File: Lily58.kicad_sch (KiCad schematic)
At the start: 14 parts, among them J1 USB_C_Receptacle, U1 ESP32-S3-WROOM-2, U3 BQ24090DGQ, U4 AP63203WU, Y1 Crystal_GND24

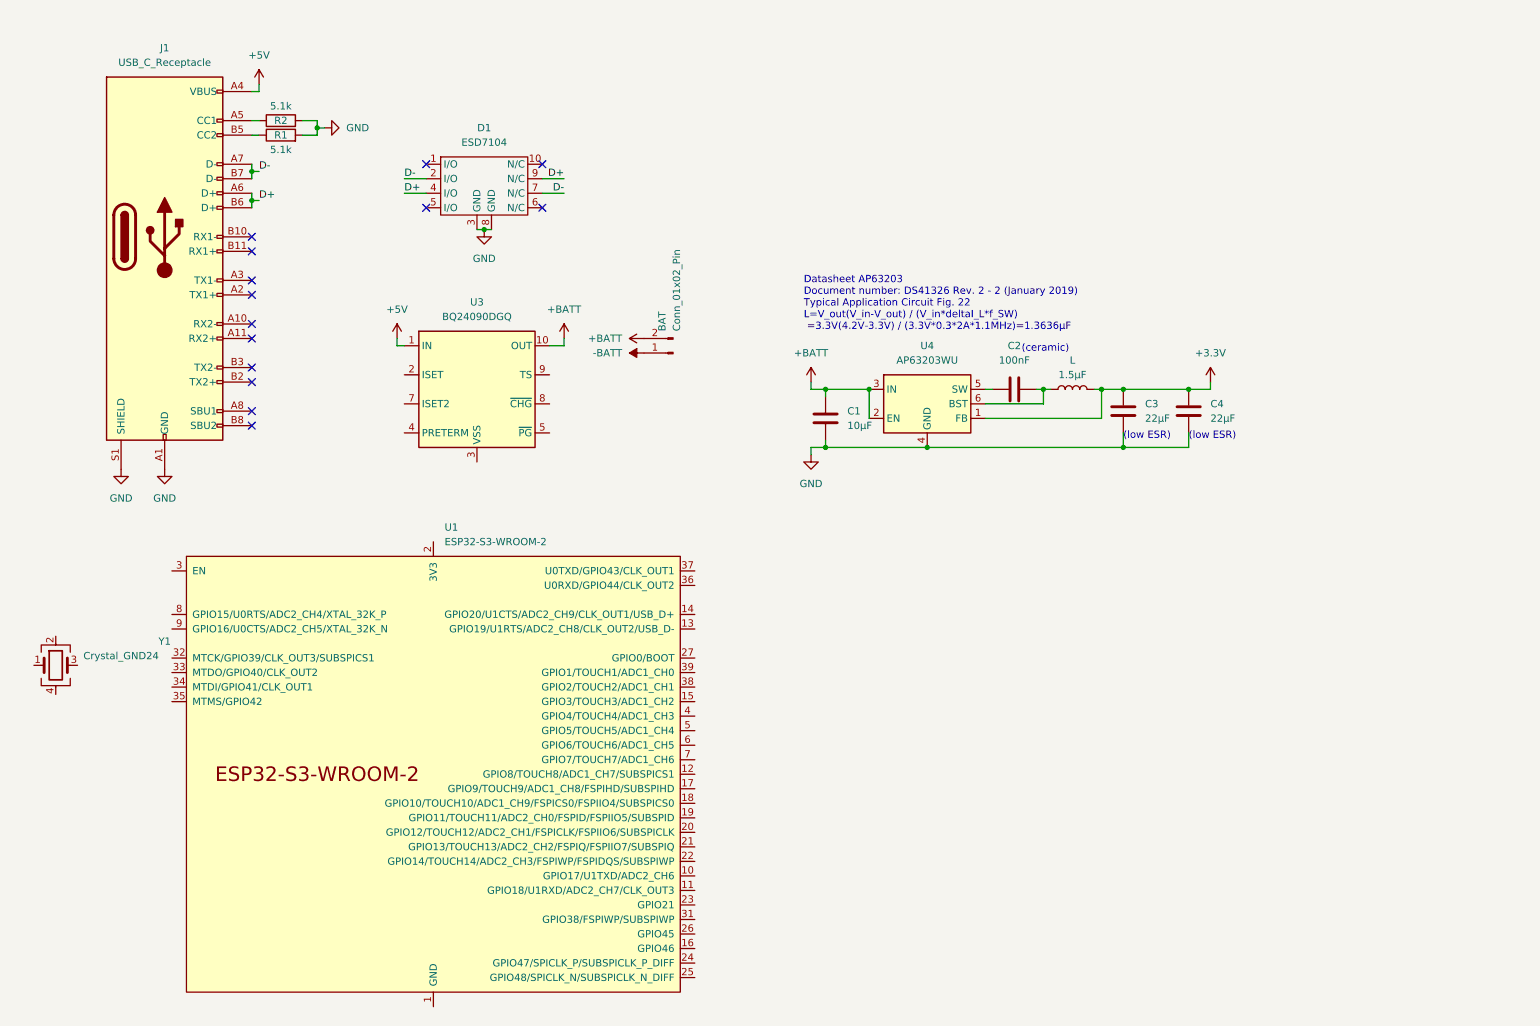
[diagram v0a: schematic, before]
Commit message: connected second USB-C receptacle; reorganized schematic
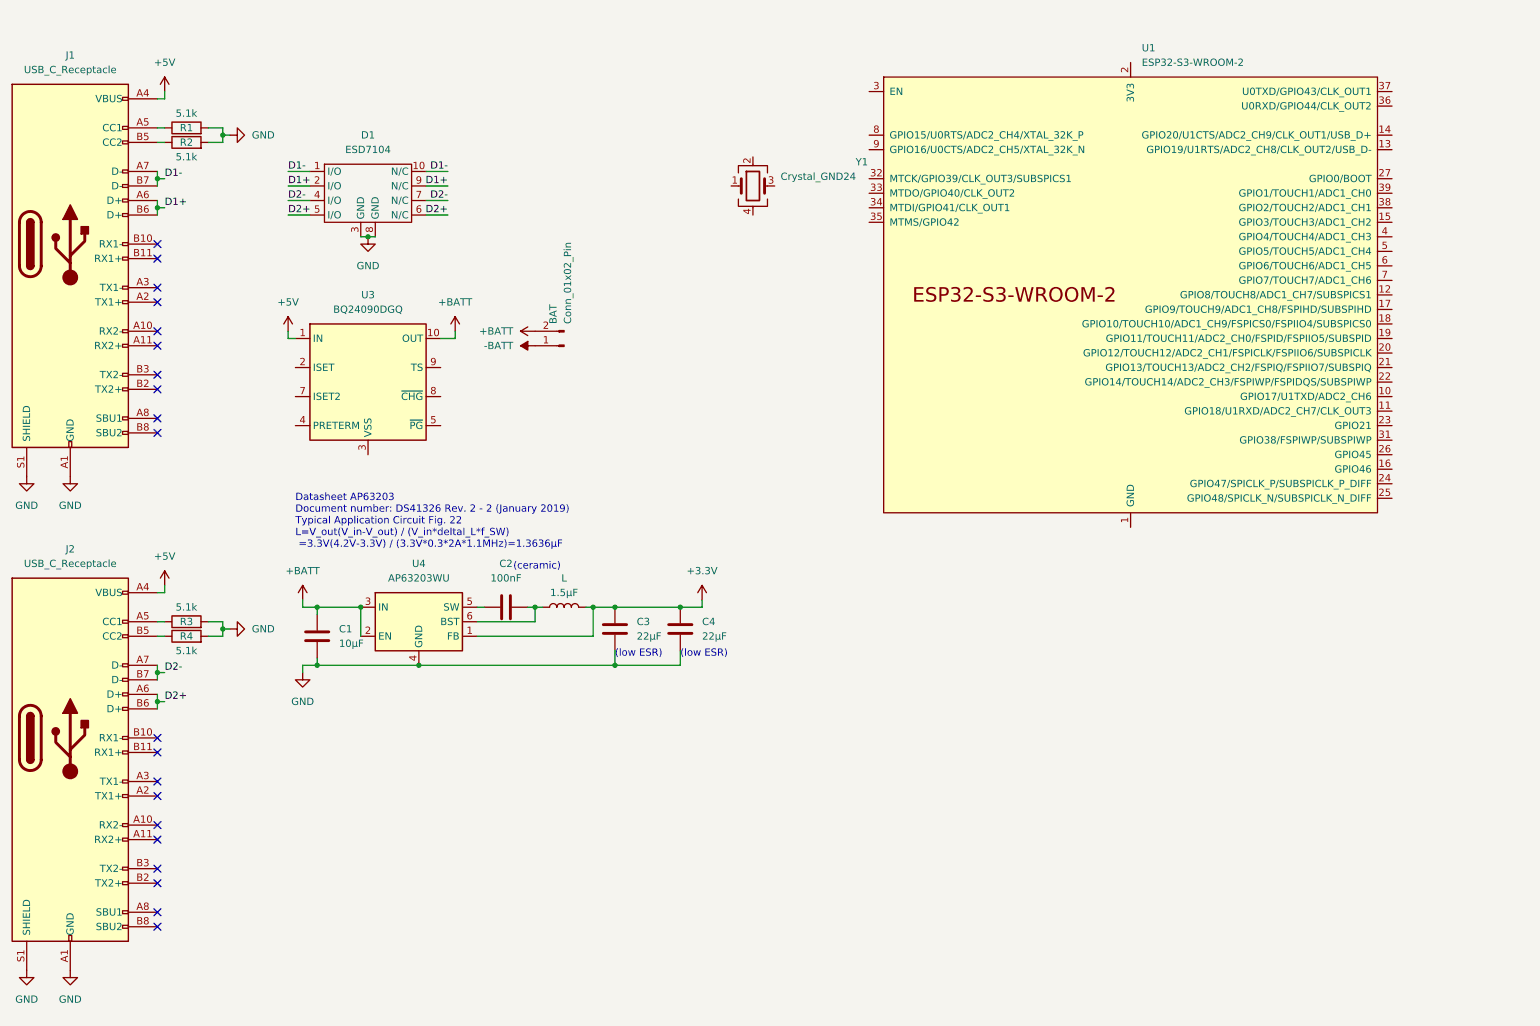
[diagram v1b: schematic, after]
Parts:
- added J2: USB_C_Receptacle, Connector_USB:USB_C_Receptacle_Amphenol_12401548E4-2A_CircularHoles, symbol Connector:USB_C_Receptacle
- added R3, R4: 5.1k, Resistor_SMD:R_0805_2012Metric_Pad1.20x1.40mm_HandSolder, symbol Device:R
- renumbered R2 to R1, R1 to R2
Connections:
- net +5V: now also J2.A4 (VBUS), J2.A9 (VBUS), J2.B4 (VBUS), J2.B9 (VBUS)
- net GND: now also J2.A1 (GND), J2.A12 (GND), J2.B1 (GND), J2.B12 (GND), J2.S1 (SHIELD), R3.2, R4.2
- net D1-: now reaches D1.1 (I/O)
- net D1-: now also D1.10 (N/C), J1.A7 (D-), J1.B7 (D-)
- net D2+: now reaches D1.5 (I/O)
- net D2+: now also D1.6 (N/C), J2.A6 (D+), J2.B6 (D+)
- net D+ renamed D1+
- net D1+: now also D1.2 (I/O); no longer D1.4 (I/O)
- removed net D-: D1.2 (I/O), D1.7 (N/C), J1.A7 (D-), J1.B7 (D-)
- new net: J2.A5 (CC1), R3.1
- new net: J2.B5 (CC2), R4.1
- new net D2-: D1.4 (I/O), D1.7 (N/C), J2.A7 (D-), J2.B7 (D-)
- no-connect marks 14 -> 20
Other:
- moved on the sheet: BAT, C1, C2, C3, C4, D1, J1, L, R1, R2, U1, U3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

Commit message: added level shifter and connected D+/D- with USB and I2C
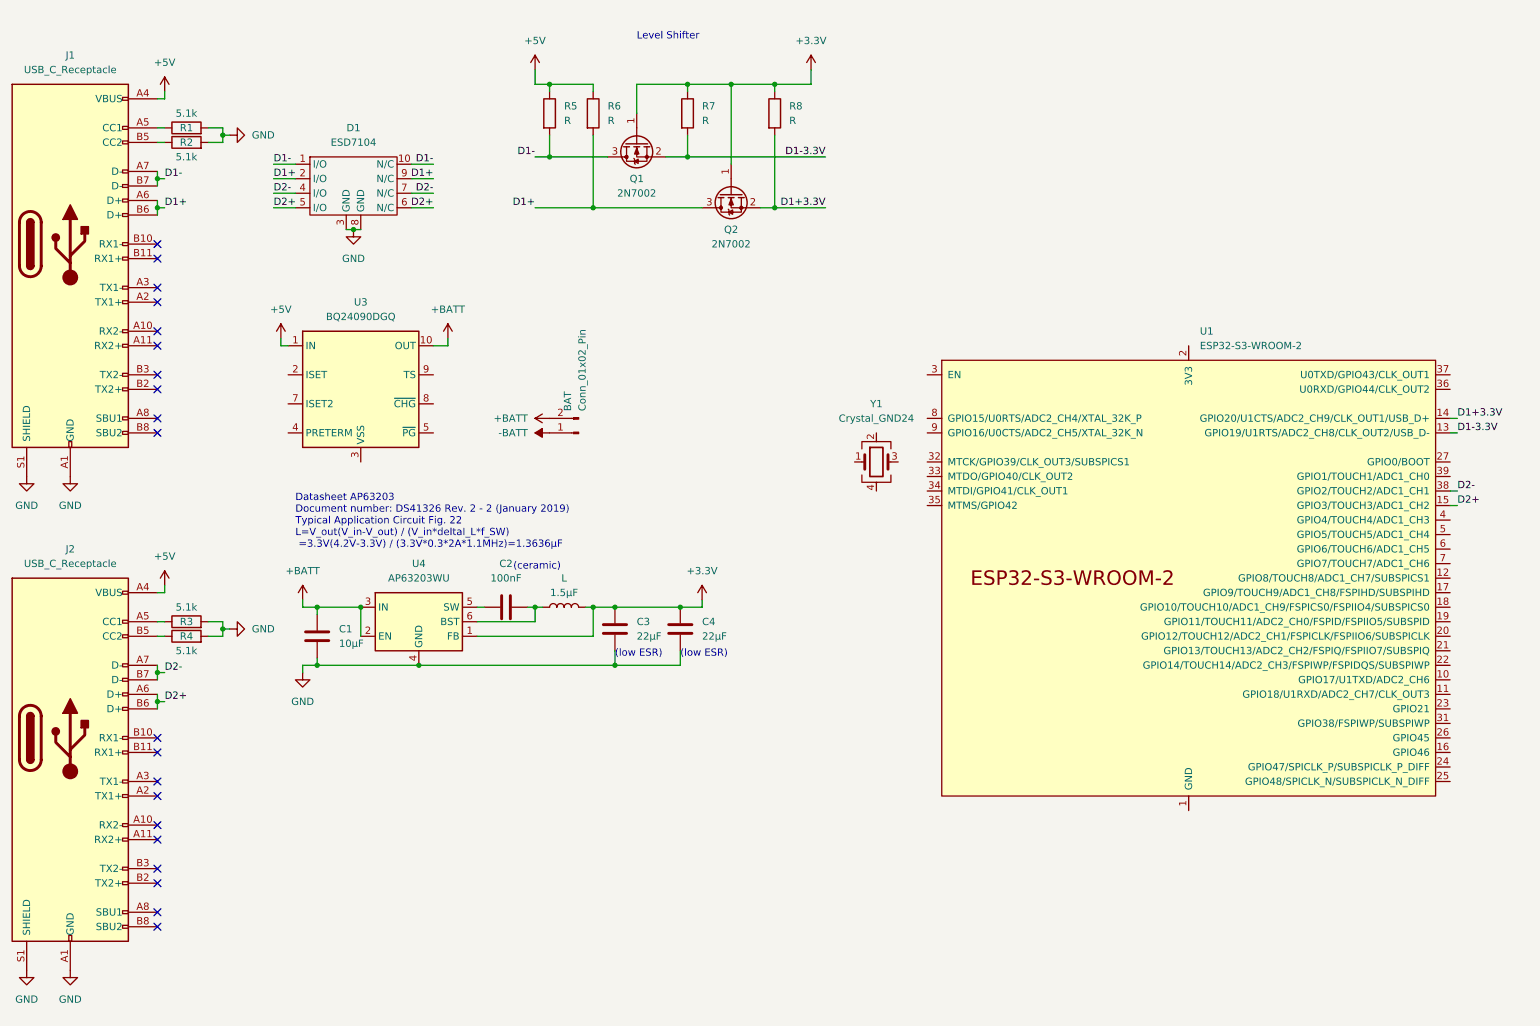
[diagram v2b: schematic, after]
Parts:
- added Q1, Q2: 2N7002, Package_TO_SOT_SMD:SOT-23, symbol Transistor_FET:2N7002
- added R5, R6, R7, R8: R, symbol Device:R
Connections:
- net +3.3V: now also Q1.1 (G), Q2.1 (G), R7.1, R8.1
- net +5V: now also R5.1, R6.1
- net D1+: now also Q2.3 (D), R6.2
- net D1-: now also Q1.3 (D), R5.2
- net D2+: now also U1.15 (GPIO3/TOUCH3/ADC1_CH2)
- net D2-: now also U1.38 (GPIO2/TOUCH2/ADC1_CH1)
- net D1-3.3V: now reaches U1.13 (GPIO19/U1RTS/ADC2_CH8/CLK_OUT2/USB_D-)
- net D1-3.3V: now also Q1.2 (S), R7.2
- net D1+3.3V: now reaches U1.14 (GPIO20/U1CTS/ADC2_CH9/CLK_OUT1/USB_D+)
- net D1+3.3V: now also Q2.2 (S), R8.2
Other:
- note added: "Level Shifter"
- moved on the sheet: BAT, D1, U1, U3, Y1

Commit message: added level shifters to second USB recaptacle for input protection
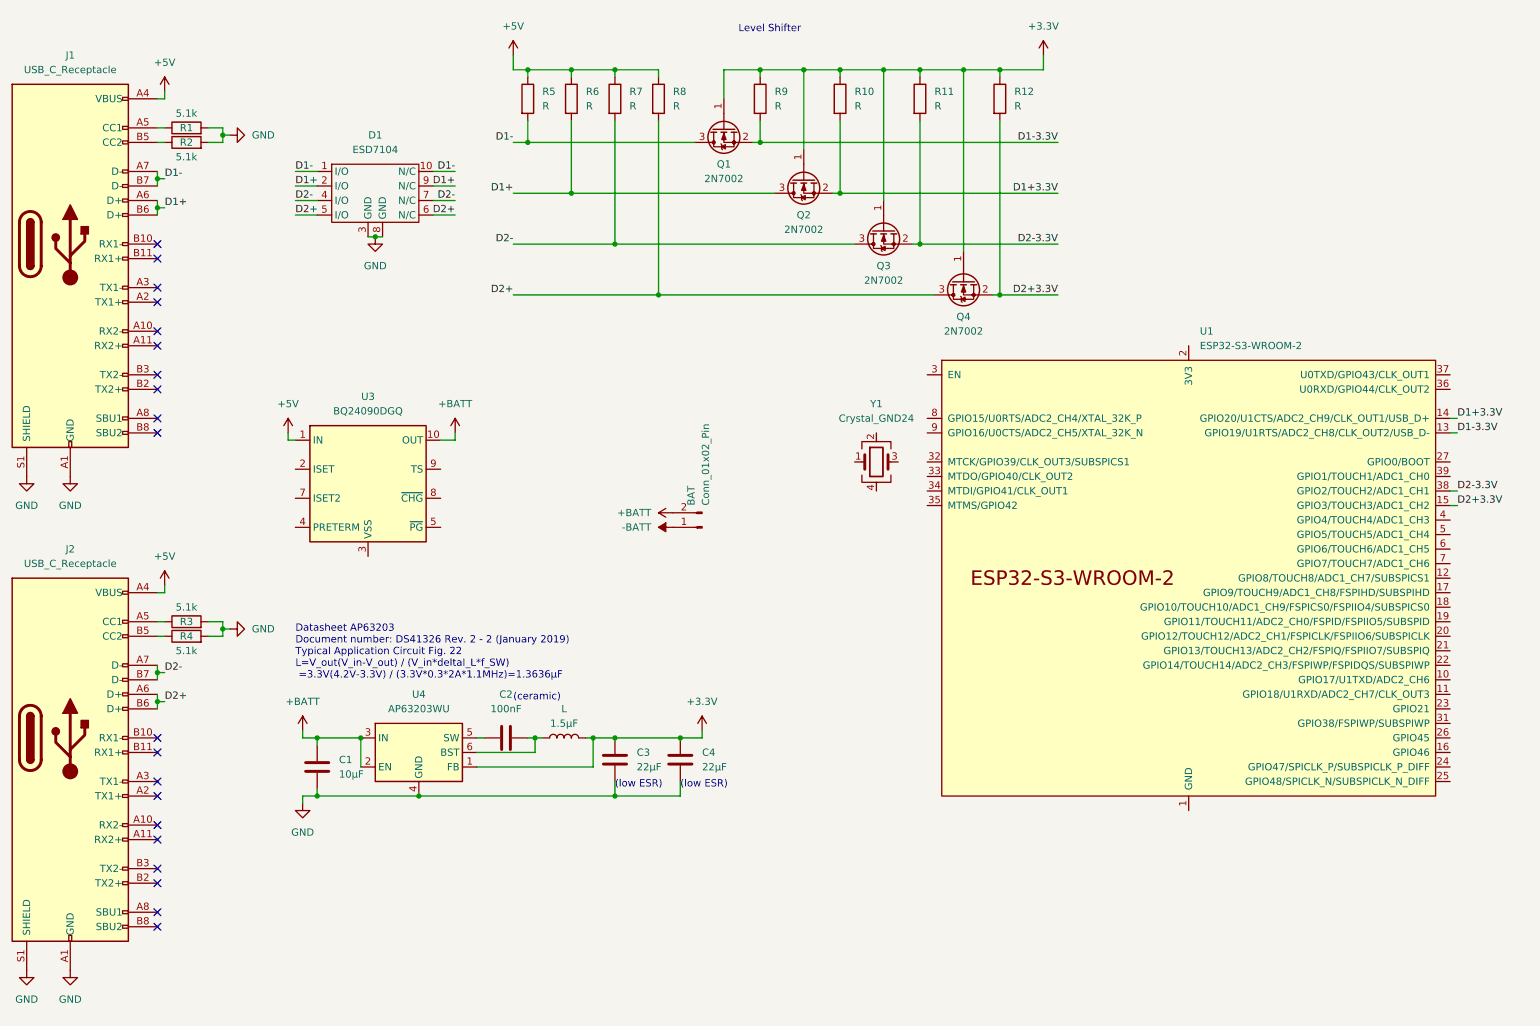
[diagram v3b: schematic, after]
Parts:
- added Q3, Q4: 2N7002, Package_TO_SOT_SMD:SOT-23, symbol Transistor_FET:2N7002
- added R11, R12, R7, R8: R, symbol Device:R
- renumbered R8 to R10, R7 to R9
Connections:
- net +3.3V: now also Q3.1 (G), Q4.1 (G), R11.1, R12.1
- net +5V: now also R7.1, R8.1
- net D2+: now also Q4.3 (D), R8.2; no longer U1.15 (GPIO3/TOUCH3/ADC1_CH2)
- net D2-: now also Q3.3 (D), R7.2; no longer U1.38 (GPIO2/TOUCH2/ADC1_CH1)
- new net D2+3.3V: Q4.2 (S), R12.2, U1.15 (GPIO3/TOUCH3/ADC1_CH2)
- new net D2-3.3V: Q3.2 (S), R11.2, U1.38 (GPIO2/TOUCH2/ADC1_CH1)
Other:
- moved on the sheet: BAT, C1, C2, C3, C4, D1, L, Q1, Q2, R10, R5, R6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

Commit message: changed AP63201 to TPS63001; added TPS63001 datasheet
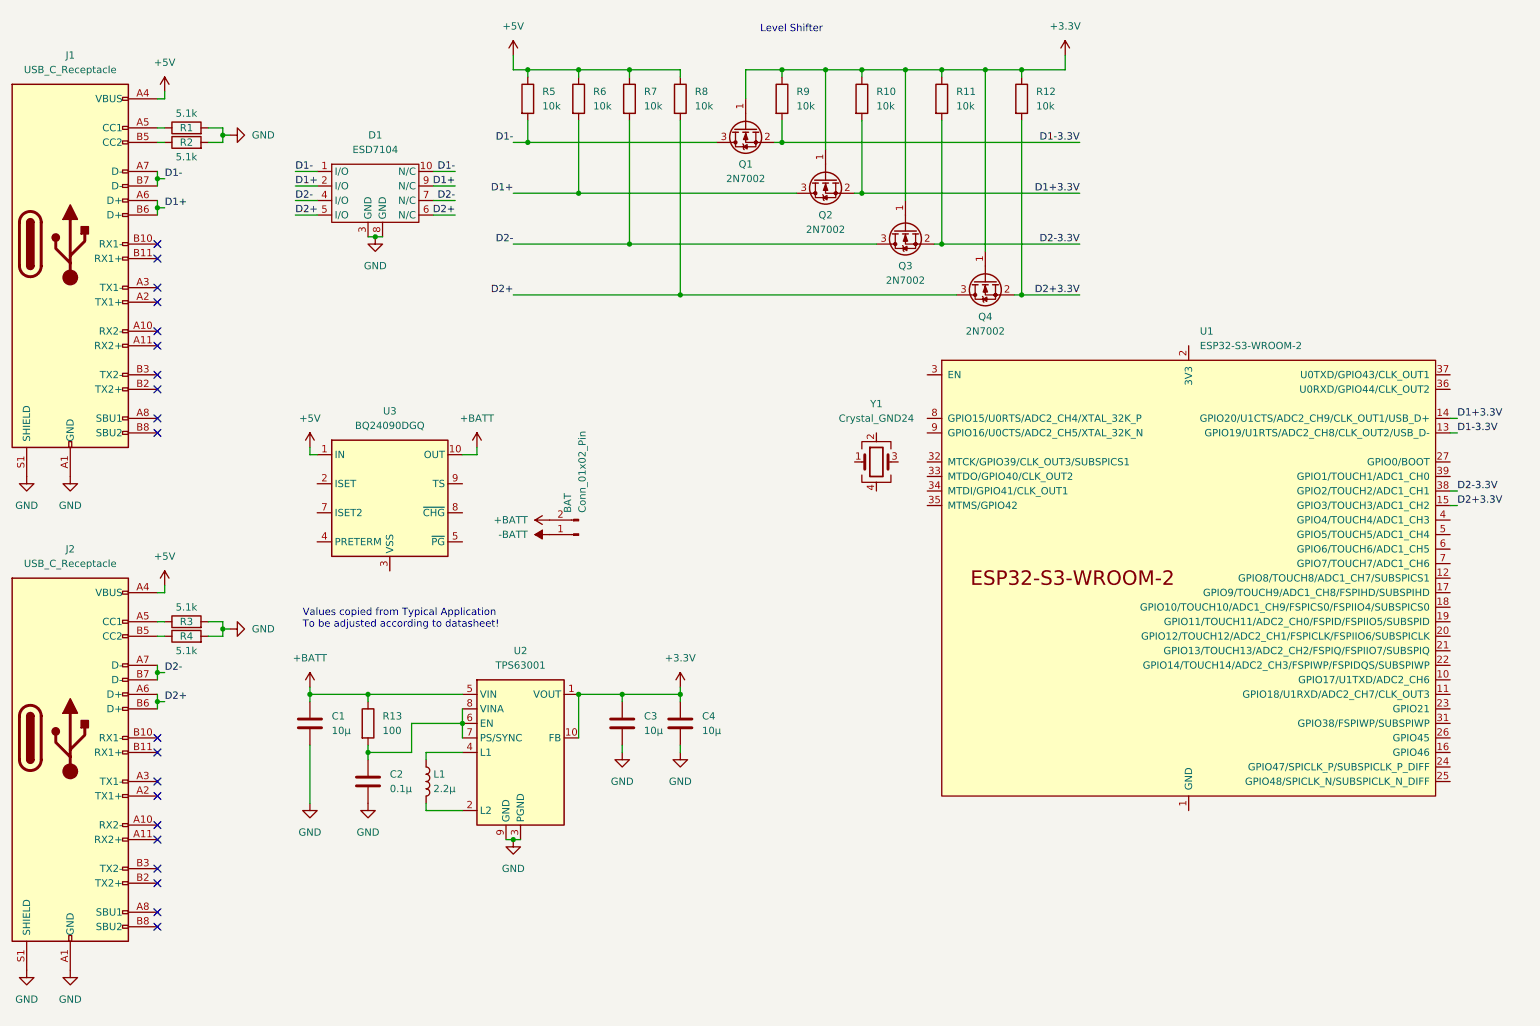
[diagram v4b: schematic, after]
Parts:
- removed L: 1.5µF, symbol Device:L
- removed U4: AP63203WU, Package_TO_SOT_SMD:TSOT-23-6, symbol Regulator_Switching:AP63203WU
- added L1: 2.2µ, symbol Device:L
- added R13: 100, symbol Device:R
- added U2: TPS63001, Package_SON:Texas_DRC0010J_ThermalVias, symbol Regulator_Switching:TPS63001
- C1: value 10µF -> 10µ
- C2: value 100nF -> 0.1µ
- C3, C4: value 22µF -> 10µ
- R10, R11, R12, R5, R6, R7, R8, R9: value R -> 10k
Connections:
- net +3.3V: now also U2.1 (VOUT), U2.10 (FB)
- net +BATT: now also R13.1, U2.5 (VIN)
- net GND: now also C2.2, U2.11 (PGND), U2.3 (PGND), U2.9 (GND)
- net at C2.1: now also R13.2, U2.6 (EN), U2.7 (PS/SYNC), U2.8 (VINA)
- new net: L1.1, U2.4 (L1)
- new net: L1.2, U2.2 (L2)
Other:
- note added: "Values copied from Typical Application To be adjusted according to datasheet!"
- note removed: "(ceramic)"
- note removed: "(low ESR)"
- note removed: "Datasheet AP63203 Document number: DS41326 Rev. 2 - 2 (January 2019) Typical Application Circuit Fig. 22 L=V_out(V_in-V_out) / (V_in*deltaI_L*f_SW) =3.3V(4.2V-3.3V) / (3.3V*0.3*2A*1.1MHz)=1.3636µF"
- moved on the sheet: BAT, Q1, Q2, Q3, Q4, R10, R11, R12, R6, R7, R8, R9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
